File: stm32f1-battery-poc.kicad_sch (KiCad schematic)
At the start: 73 parts, among them J1 Conn_02x07_Odd_Even, J2 Conn_01x02, Q1 Q_NMOS, Q2 Q_NMOS, SW1 SW_Push, SW2 SW_Push, SW3 SW_Push, SW4 SW_SPST, U1 STM32F103C8Tx, U2 SN65HVD230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

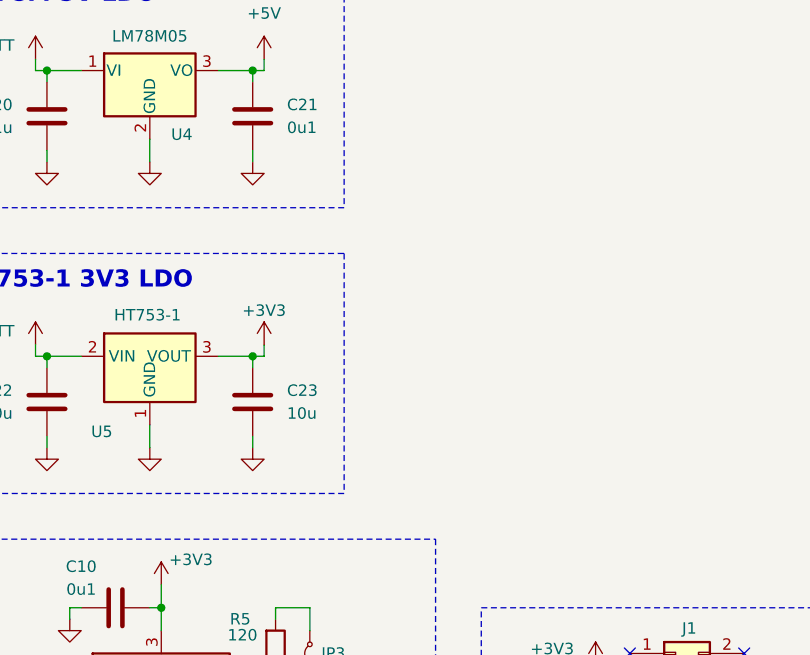
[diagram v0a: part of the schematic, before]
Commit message: schem: add 3V3 ldo select
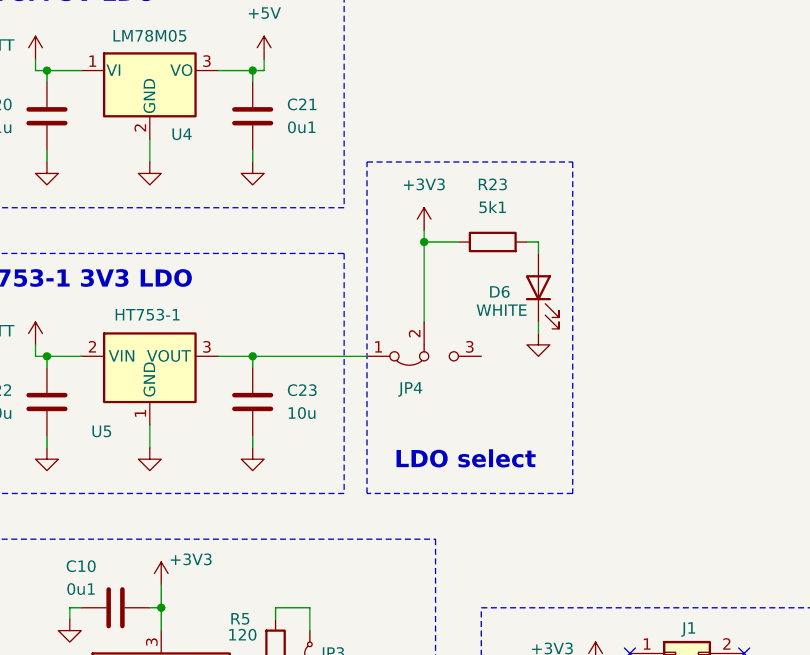
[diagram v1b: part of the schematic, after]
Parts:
- added D6: WHITE, LED_SMD:LED_0603_1608Metric, symbol Device:LED
- added JP4: Jumper_3_Bridged12, Connector_PinHeader_2.54mm:PinHeader_1x03_P2.54mm_Vertical, symbol Jumper:Jumper_3_Bridged12
- added R23: 5k1, Resistor_SMD:R_0402_1005Metric, symbol Device:R
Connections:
- net +3V3: now also JP4.2 (C), R23.1; no longer C23.1, U5.3 (VOUT)
- net GND: now also D6.1 (K)
- new net: C23.1, JP4.1 (A), U5.3 (VOUT)
- new net: D6.2 (A), R23.2
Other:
- note added: "LDO select"

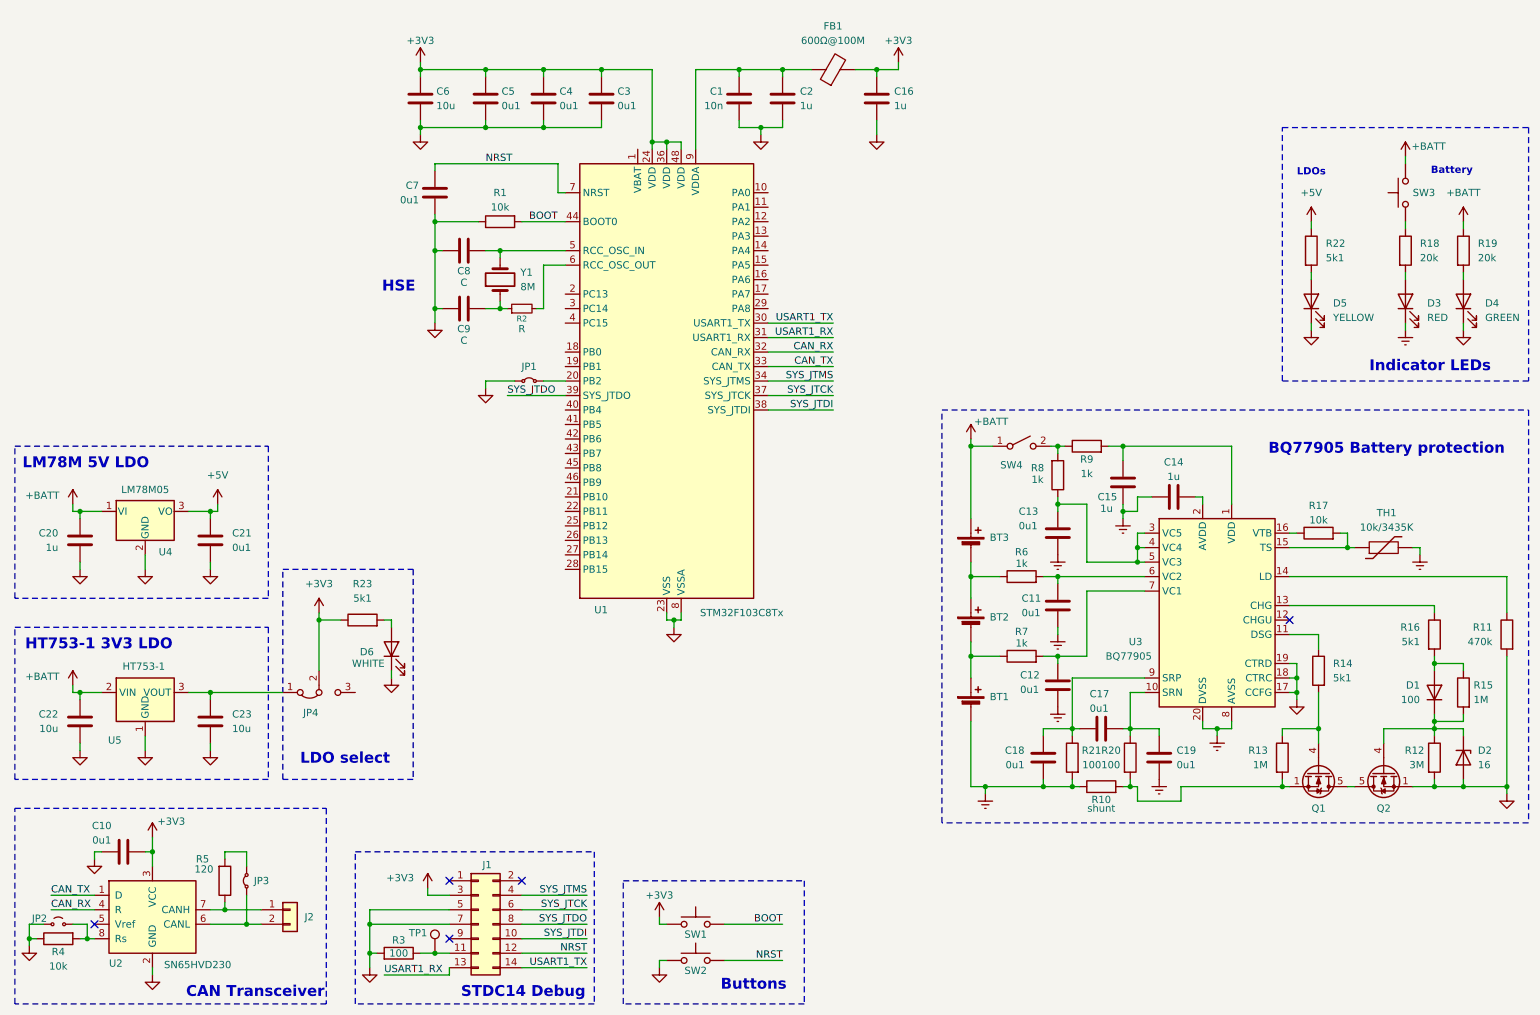
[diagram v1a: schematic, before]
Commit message: schem: add 12V power input
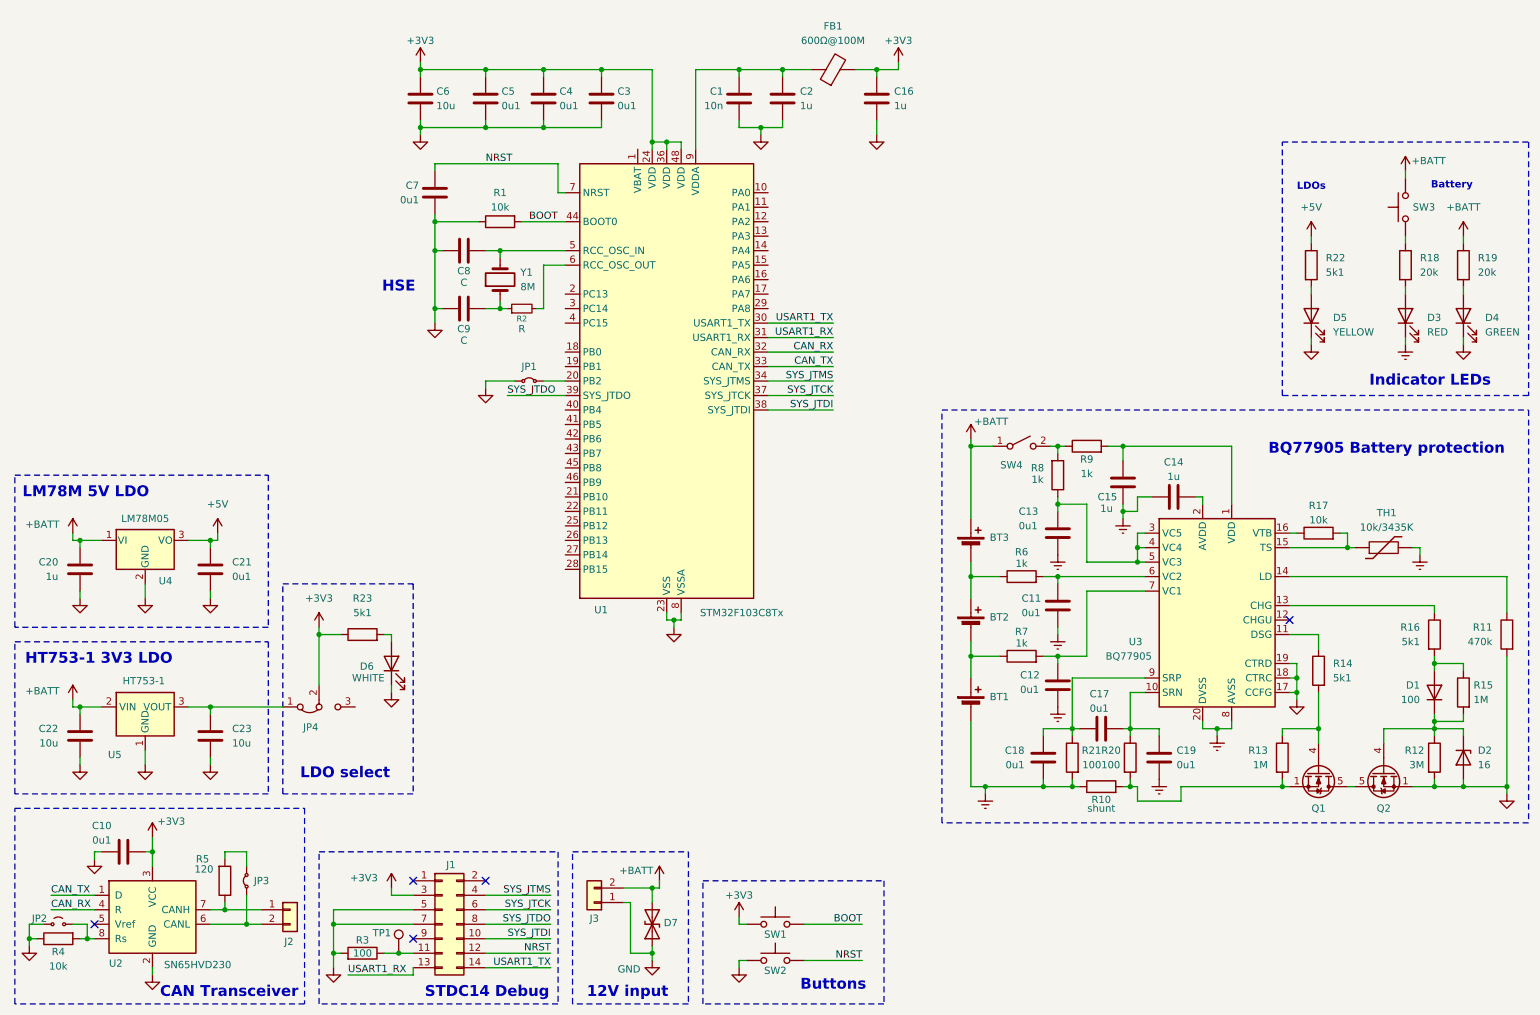
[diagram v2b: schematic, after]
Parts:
- added D7: D_TVS, Diode_SMD:D_SMB, symbol Device:D_TVS
- added J3: Conn_01x02, TerminalBlock_Phoenix:TerminalBlock_Phoenix_MKDS-1,5-2-5.08_1x02_P5.08mm_Horizontal, symbol Connector_Generic:Conn_01x02
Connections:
- net +BATT: now also D7.2 (A2), J3.2 (Pin_2)
- net GND: now also D7.1 (A1), J3.1 (Pin_1)
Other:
- note added: "12V input"
- moved on the sheet: C20, C21, C22, C23, D3, D4, D5, D6, J1, JP4, R18, R19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

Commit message: schem: add DRV8311 bldc driver
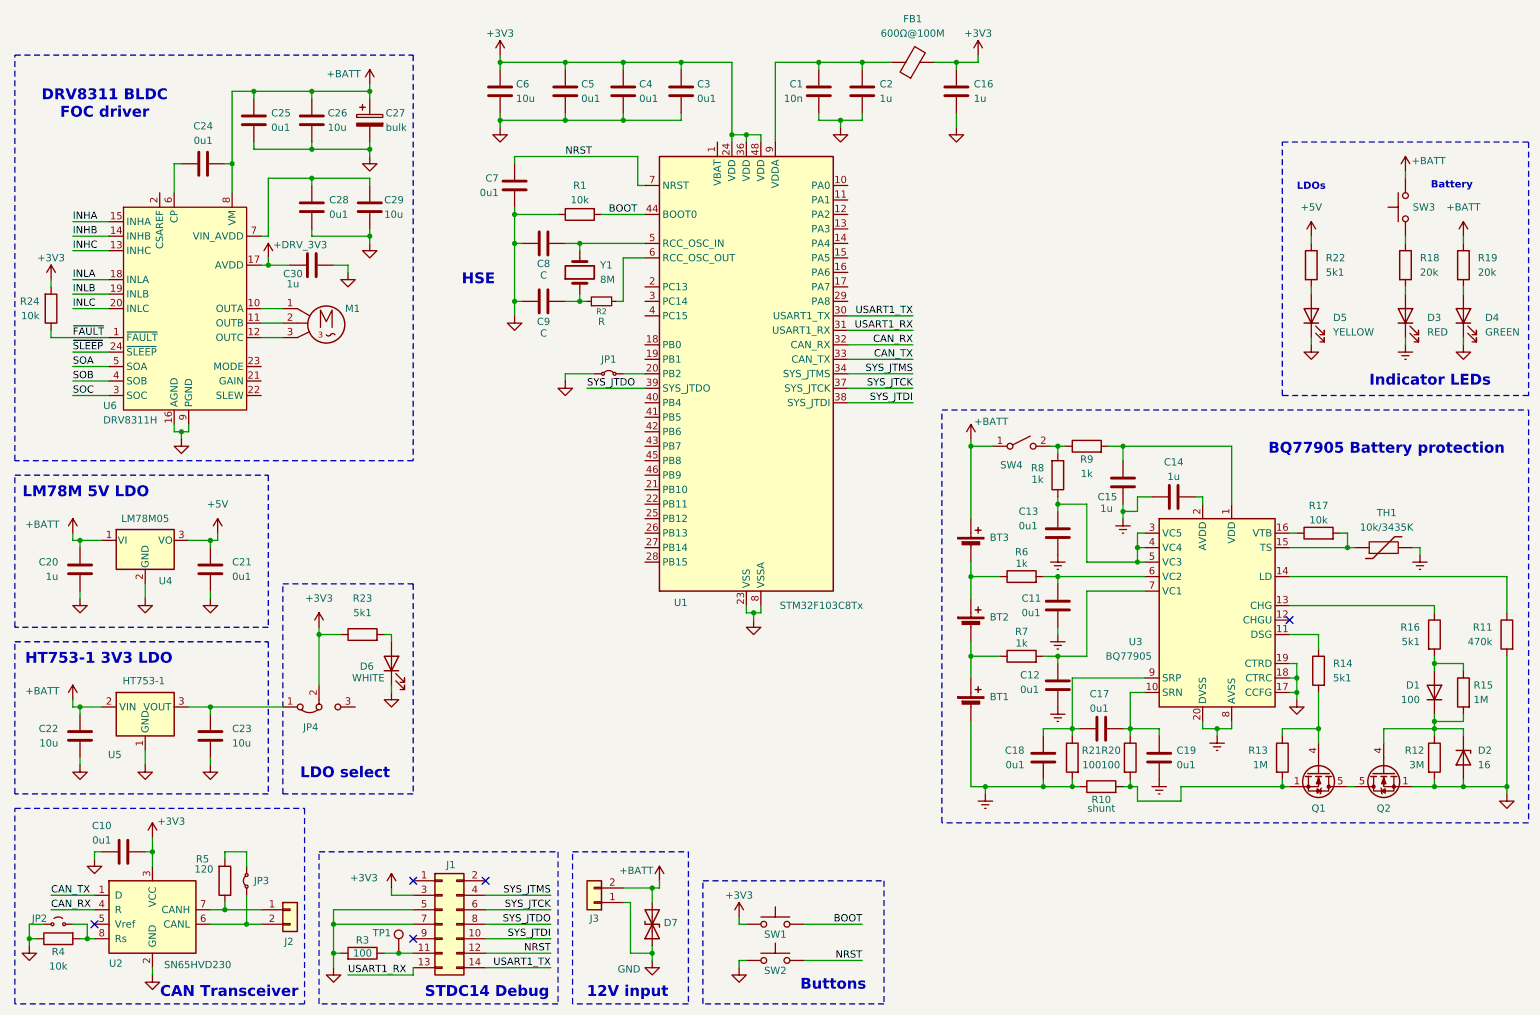
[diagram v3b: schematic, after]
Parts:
- added C24, C25, C28: 0u1, symbol Device:C
- added C26, C29: 10u, symbol Device:C
- added C27: bulk, symbol Device:C_Polarized
- added C30: 1u, symbol Device:C
- added M1: Motor_3_Phases, symbol GLCS:Motor_3_Phases
- added R24: 10k, symbol Device:R
- added U6: DRV8311H, symbol GLCS:DRV8311H
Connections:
- net +3V3: now also R24.2
- net +BATT: now also C24.2, C25.2, C26.2, C27.1, U6.8 (VM)
- net GND renamed EPAD
- net EPAD: now also C25.1, C26.1, C27.2, C28.1, C29.1, C30.2, U6.16 (AGND), U6.25 (EPAD), U6.9 (PGND)
- new net: M1.1, U6.10 (OUTA)
- new net: M1.2, U6.11 (OUTB)
- new net: M1.3, U6.12 (OUTC)
- new net: C24.1, U6.6 (CP)
- new net: C28.2, C29.2, U6.7 (VIN_AVDD)
- new net +DRV_3V3: C30.1, U6.17 (AVDD)
- new net INHA: U6.15 (INHA)
- new net INHB: U6.14 (INHB)
- new net INHC: U6.13 (INHC)
- new net INLA: U6.18 (INLA)
- new net INLB: U6.19 (INLB)
- new net INLC: U6.20 (INLC)
- new net SOA: U6.5 (SOA)
- new net SOB: U6.4 (SOB)
- new net SOC: U6.3 (SOC)
- new net ~{FAULT}: R24.1, U6.1 (~{FAULT})
- new net ~{SLEEP}: U6.24 (~{SLEEP})
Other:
- note added: "DRV8311 BLDC FOC driver"
- moved on the sheet: C1, C16, C2, C3, C4, C5, C6, C7, C8, C9, FB1, JP1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

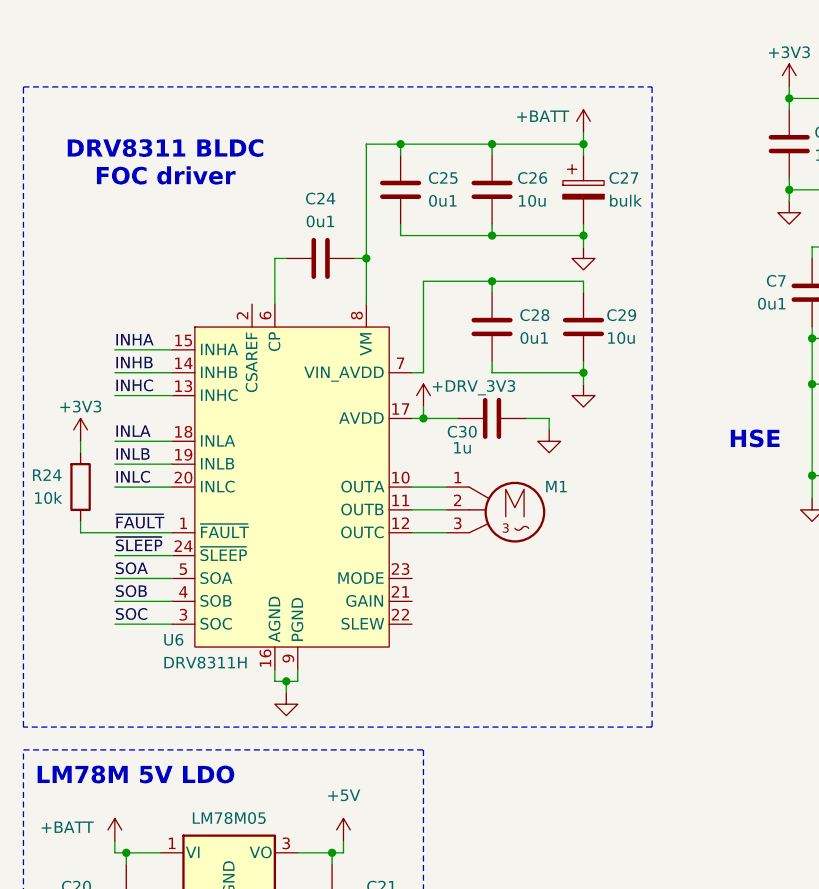
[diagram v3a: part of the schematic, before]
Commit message: schem: add DRV8311 hardware pin config jumpers
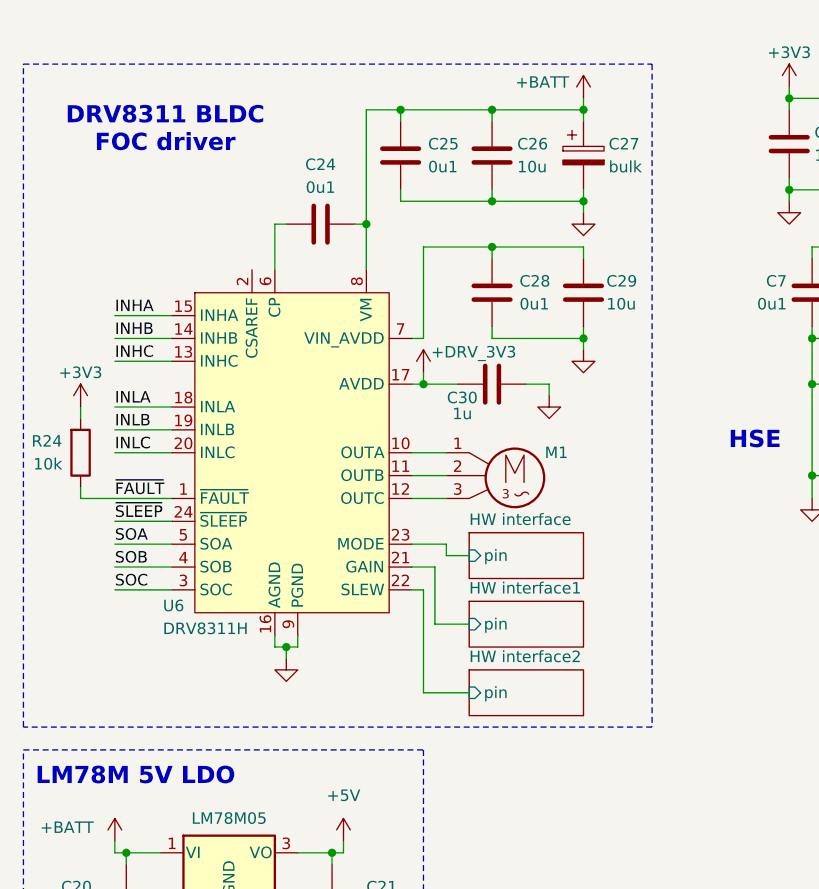
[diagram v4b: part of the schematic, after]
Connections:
- net HW interface1/pin: now reaches U6.21 (GAIN)
- net HW interface2/pin: now reaches U6.22 (SLEW)
- net HW interface/pin: now reaches U6.23 (MODE)
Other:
- added sheet HW interface (drv-hw-interface.kicad_sch)
- added sheet HW interface1 (drv-hw-interface.kicad_sch)
- added sheet HW interface2 (drv-hw-interface.kicad_sch)
- moved on the sheet: C24, C25, C26, C27, C28, C29, C30, M1, R24, U6
